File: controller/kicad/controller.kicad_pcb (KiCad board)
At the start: 2 copper layers, 90 x 88.4 mm, 33 parts, among them J1 pcie_98, J2 USB_C_Receptacle_USB2.0, U1 WeAct_STM32H750_Module, U10 ESD5344D, U11 ESD5344D, U12 ESD5344D, U13 ESD5344D, U14 ESD5344D, U15 ESD5344D, U16 CP2102N-A01-GQFN28-Interface_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, U2 ESD5344D, U3 ESD5344D, U4 ESD5344D, U5 ESD5344D, U6 ESD5344D, U7 ESD5344D, U8 ESD5344D, U9 ESD5344D

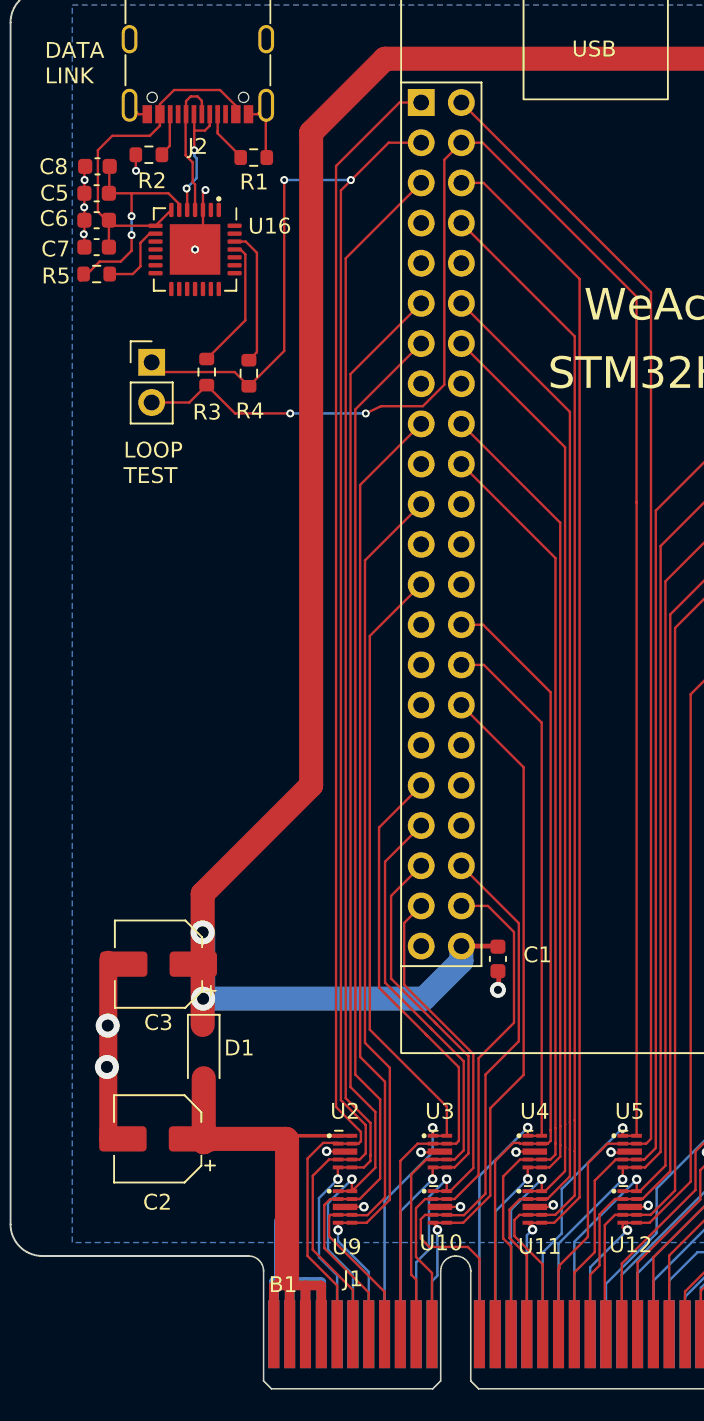
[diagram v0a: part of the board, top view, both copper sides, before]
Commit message: Cleaned up a few traces, move the power supply caps.
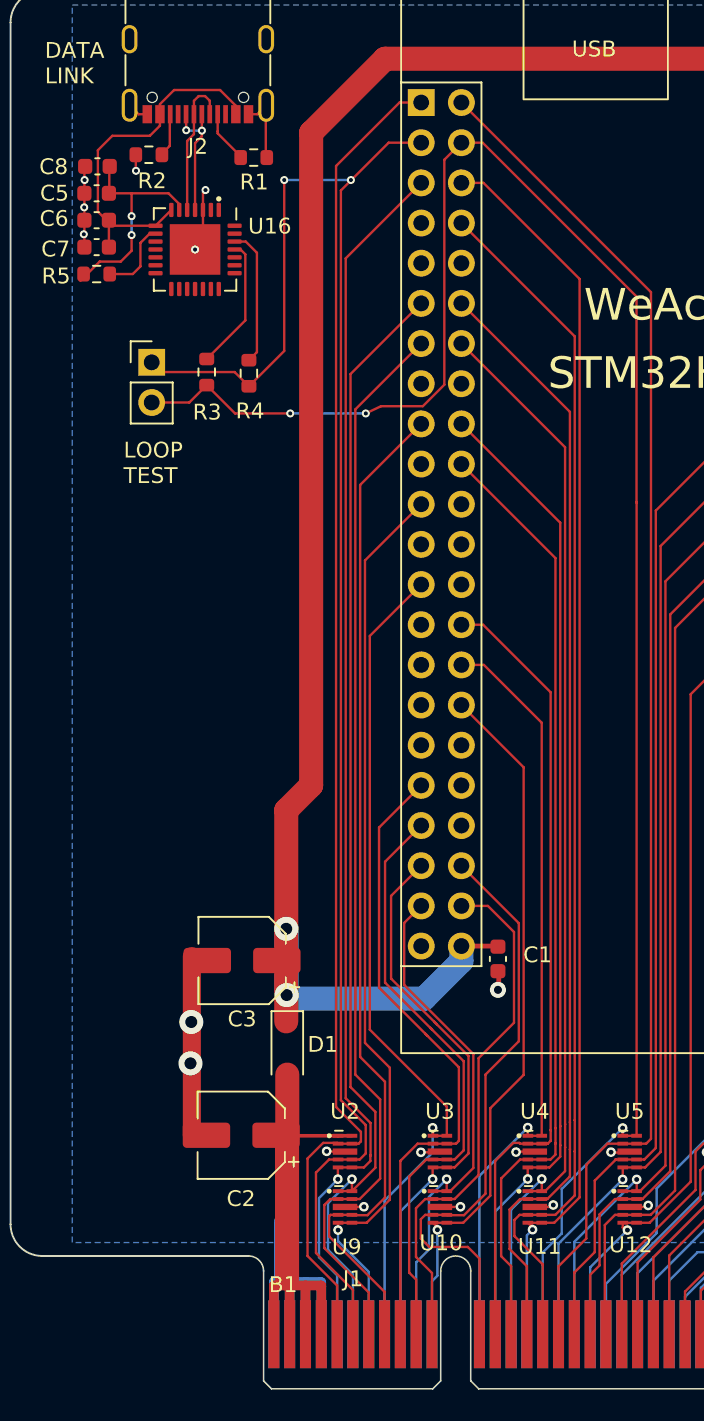
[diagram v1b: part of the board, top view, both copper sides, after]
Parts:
- moved C2 5.29 mm to (56.4, 44.0)
- moved C3 5.29 mm to (56.5, 32.9)
- moved D1 5.29 mm to (59.4, 38.5)
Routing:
- net /+5V: track 140.0 -> 132.4 mm
- net /+5VBUS: track 37.8 -> 32.5 mm
- net Net-(U16-D-): track 8.29 -> 9.17 mm, vias 2 -> 0
- net Net-(U16-D+): track 9.11 -> 8.25 mm, vias 0 -> 2

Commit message: Updated part number of a 1uf cap.
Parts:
- C1, C4: value 1uf -> 1u
- C2, C3: value 100uf -> 100u
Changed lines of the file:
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@@
     (descr "Capacitor SMD 0603 (1608 Metric), square (rectangular) end terminal, IPC_7351 nominal, (Body size source: IPC-SM-782 page 76, https://www.pcb-3d.com/wordpress/wp-content/uploads/ipc-sm-782a_amendment_1_and_2.pdf), generated with kicad-footprint-generator")
     (tags "capacitor")
-    (property "LCSC" "C106219")
+    (property "LCSC" "C15849")
     (property "Sheetfile" "controller.kicad_sch")
     (property "Sheetname" "")
@@
         (effects (font (size 1 1) (thickness 0.15)))
     )
-    (fp_text value "1uf" (at 0 1.43) (layer "F.Fab")
+    (fp_text value "1u" (at 0 1.43) (layer "F.Fab")
         (effects (font (size 1 1) (thickness 0.15)))
     )
@@
     (descr "Capacitor SMD 0603 (1608 Metric), square (rectangular) end terminal, IPC_7351 nominal, (Body size source: IPC-SM-782 page 76, https://www.pcb-3d.com/wordpress/wp-content/uploads/ipc-sm-782a_amendment_1_and_2.pdf), generated with kicad-footprint-generator")
     (tags "capacitor")
-    (property "LCSC" "C106219")
+    (property "LCSC" "C15849")
     (property "Sheetfile" "controller.kicad_sch")
     (property "Sheetname" "")
@@
         (effects (font (size 1 1) (thickness 0.15)))
     )
-    (fp_text value "1uf" (at 0 1.43 -90) (layer "F.Fab")
+    (fp_text value "1u" (at 0 1.43 -90) (layer "F.Fab")
         (effects (font (size 1 1) (thickness 0.15)))
     )
@@
         (effects (font (size 1 1) (thickness 0.15)))
     )
-    (fp_text value "100uf" (at 0 -3.7) (layer "F.Fab")
+    (fp_text value "100u" (at 0 -3.7) (layer "F.Fab")
         (effects (font (size 1 1) (thickness 0.15)))
     )
@@
         (effects (font (size 1 1) (thickness 0.15)))
     )
-    (fp_text value "100uf" (at 0 -3.7) (layer "F.Fab")
-        (effects (font (size 1 1) (thickness 0.15)))
-    )
+    (fp_text value "100u" (at 0 -3.7) (layer "F.Fab")
+        (effects (font (size 1 1) (thickness 0.15)))
+    )

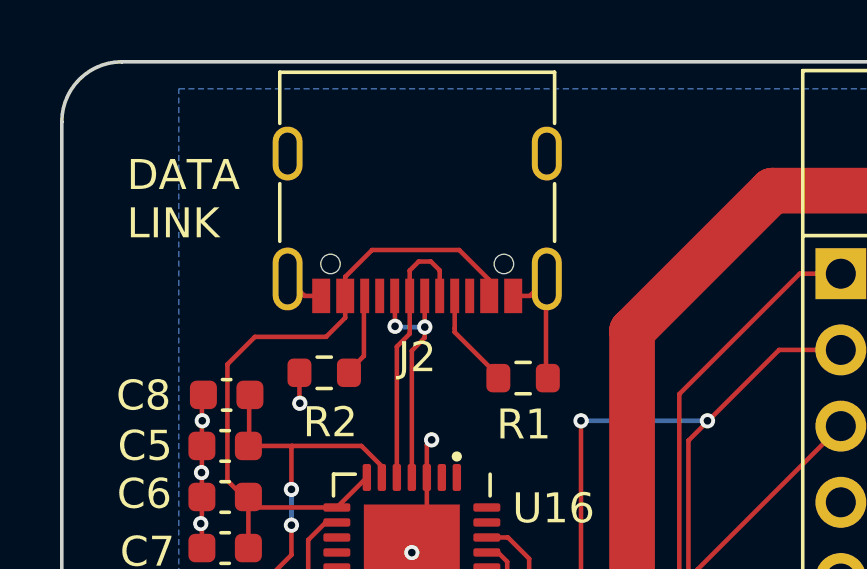
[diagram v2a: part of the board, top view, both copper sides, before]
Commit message: Moved the USB connector closer to the board edge.
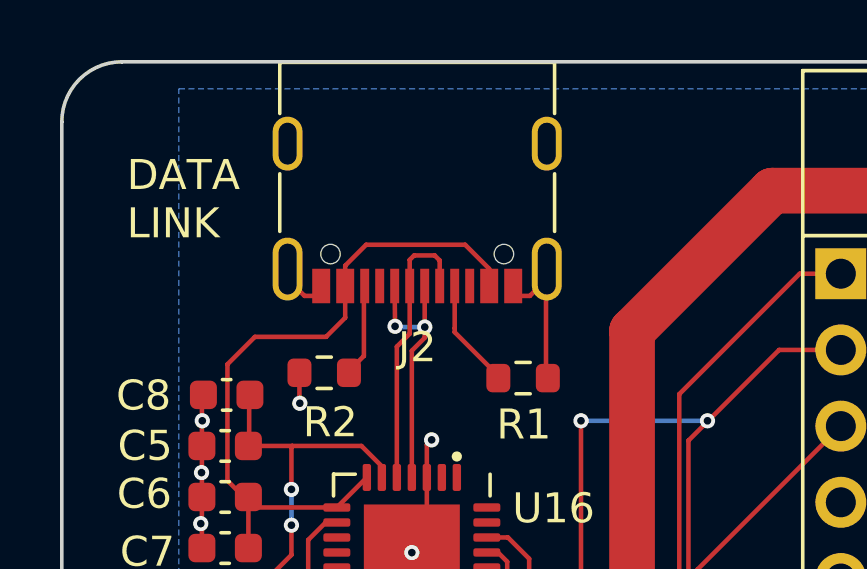
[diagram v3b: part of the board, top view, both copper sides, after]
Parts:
- moved J2 0.33 mm to (53.7, -23.1)
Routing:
- net Net-(J2-VBUS): track 23.1 -> 23.6 mm
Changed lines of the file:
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@@
   )
   (footprint "controller:USB_C_Receptacle_XKB_U262-16XN-4BVC11" (layer "F.Cu")
-    (at 53.6967 -22.7663 180)
+    (at 53.6967 -23.0965 180)
     (descr "USB Type C, right-angle, SMT, https://datasheet.lcsc.com/szlcsc/1811141824_XKB-Enterprise-U262-161N-4BVC11_C319148.pdf")
     (tags "USB C Type-C Receptacle SMD")
@@
   (via (at 49.5046 -14.1478) (size 0.508) (drill 0.254) (layers "F.Cu" "B.Cu") (net 120))
   (segment (start 49.5046 -12.954) (end 49.5046 -14.1478) (width 0.1524) (layer "B.Cu") (net 120))
+  (segment (start 48.2865 -19.2315) (end 47.371 -18.316) (width 0.1524) (layer "F.Cu") (net 121))
   (segment (start 47.371 -18.316) (end 47.371 -14.4402) (width 0.1524) (layer "F.Cu") (net 121))
-  (segment (start 56.0967 -21.1285) (end 55.0981 -22.1271) (width 0.1524) (layer "F.Cu") (net 121))
-  (segment (start 51.2967 -20.5963) (end 51.2967 -19.8689) (width 0.1524) (layer "F.Cu") (net 121))
-  (segment (start 56.0967 -20.5963) (end 56.0967 -21.1285) (width 0.1524) (layer "F.Cu") (net 121))
-  (segment (start 51.2967 -21.230364) (end 51.2967 -20.5963) (width 0.1524) (layer "F.Cu") (net 121))
-  (segment (start 55.0981 -22.1271) (end 52.193436 -22.1271) (width 0.1524) (layer "F.Cu") (net 121))
+  (segment (start 55.2958 -22.3012) (end 51.9938 -22.3012) (width 0.1524) (layer "F.Cu") (net 121))
+  (segment (start 47.371 -14.4402) (end 48.2671 -13.5441) (width 0.1524) (layer "F.Cu") (net 121))
   (segment (start 48.2671 -13.5441) (end 51.0178 -13.5441) (width 0.1524) (layer "F.Cu") (net 121))
+  (segment (start 51.2967 -21.6041) (end 51.2967 -20.9265) (width 0.1524) (layer "F.Cu") (net 121))
+  (segment (start 51.2967 -21.230364) (end 51.2967 -19.8689) (width 0.1524) (layer "F.Cu") (net 121))
+  (segment (start 56.0967 -21.5003) (end 55.2958 -22.3012) (width 0.1524) (layer "F.Cu") (net 121))
+  (segment (start 52.0178 -14.5441) (end 51.0178 -13.5441) (width 0.1524) (layer "F.Cu") (net 121))
+  (segment (start 56.0967 -20.9265) (end 56.0967 -21.5003) (width 0.1524) (layer "F.Cu") (net 121))
+  (segment (start 48.0698 -13.8938) (end 48.0698 -12.192) (width 0.1524) (layer "F.Cu") (net 121))
   (segment (start 50.6593 -19.2315) (end 48.2865 -19.2315) (width 0.1524) (layer "F.Cu") (net 121))
   (segment (start 51.2967 -19.8689) (end 50.6593 -19.2315) (width 0.1524) (layer "F.Cu") (net 121))
-  (segment (start 47.371 -14.4402) (end 48.2671 -13.5441) (width 0.1524) (layer "F.Cu") (net 121))
-  (segment (start 52.193436 -22.1271) (end 51.2967 -21.230364) (width 0.1524) (layer "F.Cu") (net 121))
-  (segment (start 48.2865 -19.2315) (end 47.371 -18.316) (width 0.1524) (layer "F.Cu") (net 121))
-  (segment (start 52.0178 -14.5441) (end 51.0178 -13.5441) (width 0.1524) (layer "F.Cu") (net 121))
-  (segment (start 48.0698 -13.8938) (end 48.0698 -12.192) (width 0.1524) (layer "F.Cu") (net 121))
+  (segment (start 51.9938 -22.3012) (end 51.2967 -21.6041) (width 0.1524) (layer "F.Cu") (net 121))
   (segment (start 54.9467 -19.5187) (end 54.9467 -19.3869) (width 0.1524) (layer "F.Cu") (net 122))
   (segment (start 54.9467 -20.5963) (end 54.9467 -19.5187) (width 0.1524) (layer "F.Cu") (net 122))
@@
   (segment (start 53.9496 -19.558) (end 52.9844 -19.558) (width 0.1524) (layer "B.Cu") (net 124))
   (segment (start 52.9844 -19.558) (end 52.959 -19.5834) (width 0.1524) (layer "B.Cu") (net 124))
-  (segment (start 53.7464 -21.7424) (end 53.4467 -21.4427) (width 0.1524) (layer "F.Cu") (net 125))
-  (segment (start 54.4467 -21.4485) (end 54.1528 -21.7424) (width 0.1524) (layer "F.Cu") (net 125))
+  (segment (start 54.4467 -21.7787) (end 54.2798 -21.9456) (width 0.1524) (layer "F.Cu") (net 125))
   (segment (start 53.0178 -18.9056) (end 53.4467 -19.3345) (width 0.1524) (layer "F.Cu") (net 125))
-  (segment (start 54.4467 -20.5963) (end 54.4467 -21.4485) (width 0.1524) (layer "F.Cu") (net 125))
-  (segment (start 54.1528 -21.7424) (end 53.7464 -21.7424) (width 0.1524) (layer "F.Cu") (net 125))
-  (segment (start 53.4467 -21.4427) (end 53.4467 -20.5963) (width 0.1524) (layer "F.Cu") (net 125))
+  (segment (start 53.4467 -21.7983) (end 53.4467 -20.9265) (width 0.1524) (layer "F.Cu") (net 125))
+  (segment (start 54.4467 -20.9265) (end 54.4467 -21.7787) (width 0.1524) (layer "F.Cu") (net 125))
+  (segment (start 54.2798 -21.9456) (end 53.594 -21.9456) (width 0.1524) (layer "F.Cu") (net 125))
+  (segment (start 53.594 -21.9456) (end 53.4467 -21.7983) (width 0.1524) (layer "F.Cu") (net 125))
   (segment (start 53.4467 -19.3345) (end 53.4467 -20.5963) (width 0.1524) (layer "F.Cu") (net 125))
   (segment (start 53.0178 -14.5441) (end 53.0178 -18.9056) (width 0.1524) (layer "F.Cu") (net 125))

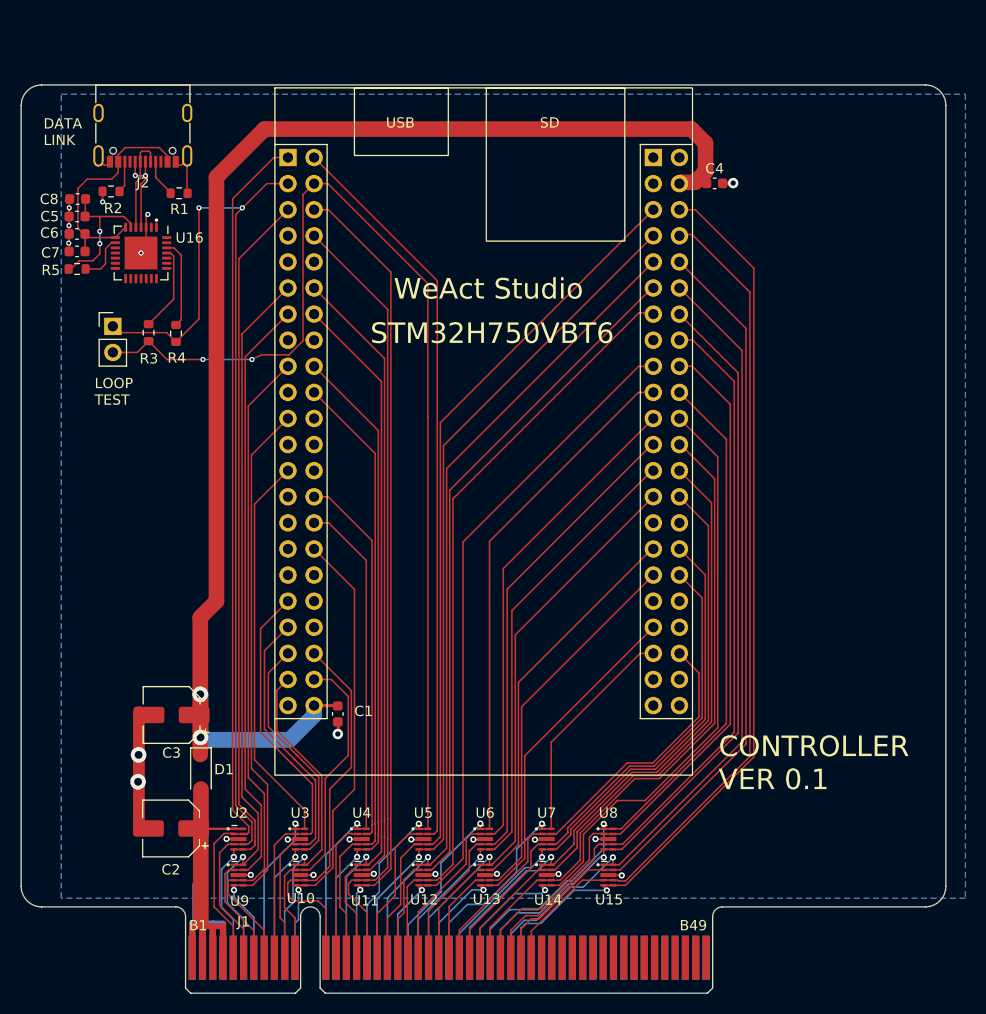
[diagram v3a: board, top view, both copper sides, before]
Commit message: Cleaning up of the controller's PCB, in progress.
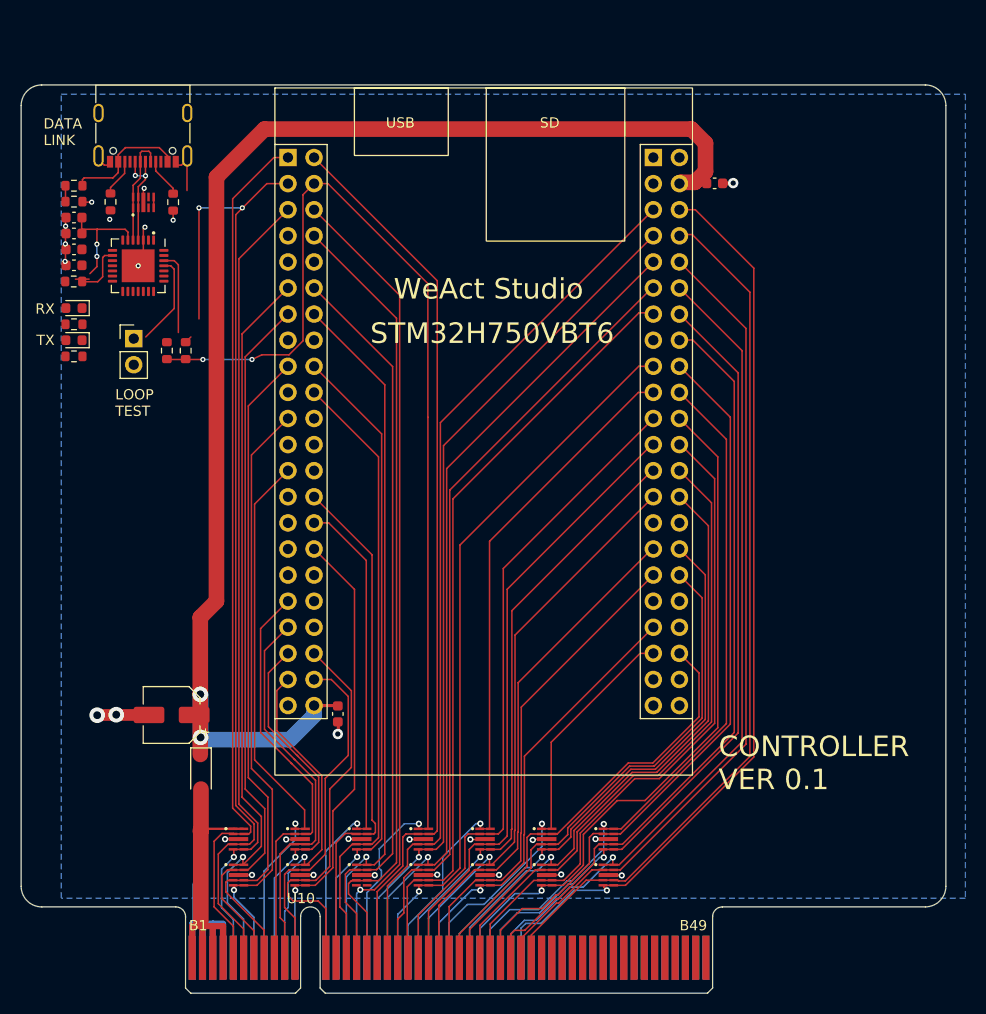
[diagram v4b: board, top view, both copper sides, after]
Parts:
- removed C2: 100u, controller:CP_Elec_5x5.4_JLCPCB
- added D2: LED YELLOW, LED_SMD:LED_0603_1608Metric, F.Cu at (47.0, -3.56)
- added D3: LED_GREEN, LED_SMD:LED_0603_1608Metric, F.Cu at (47.0, -6.68)
- added R6: 47K, Resistor_SMD:R_0603_1608Metric, F.Cu at (47.0, -17.0)
- added R7: 22K, Resistor_SMD:R_0603_1608Metric, F.Cu at (47.0, -18.6)
- added R8: 5K1, Resistor_SMD:R_0603_1608Metric, F.Cu at (47.0, -1.98)
- added R9: 5K1, Resistor_SMD:R_0603_1608Metric, F.Cu at (47.0, -5.11)
- added U17: ESD5344D, common:Diodes_UDFN-10_1.0x2.5mm_P0.5mm, F.Cu at (53.7, -17.0)
- U16: value CP2102N-A01-GQFN28-Interface_USB -> CP2102N-A02-GQFN28R
- moved R3 2.50 mm to (56.0, -2.54)
- moved JP1 2.36 mm to (52.8, -3.71)
- moved R4 1.92 mm to (57.9, -2.54)
- moved C8 1.84 mm to (47.0, -15.5)
- moved C5 1.68 mm to (47.0, -13.9)
- moved C6 1.53 mm to (47.0, -12.4)
- moved C7 1.38 mm to (47.0, -10.8)
- moved U16 1.28 mm to (53.2, -10.8)
- moved R5 1.26 mm to (47.0, -9.27)
- moved R1 1.04 mm to (56.6, -17.0), turned to -90 degrees
- moved R2 1.02 mm to (50.5, -17.0), turned to -90 degrees
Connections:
- C6 pad 2: Net-(J2-VBUS) -> /+5V
- C7 pad 2: Net-(J2-VBUS) -> /+5V
- JP1 pad 1: /PB15 -> /PA10
- JP1 pad 2: /PB14 -> /PA9
- R3 pad 2: /PB14 -> /PA9
- R4 pad 2: /PB15 -> /PA10
- U1 pad 80: unconnected-(U1B-NRST-Pad80) -> /NRST
- U16 pad 18: unconnected-(U16-~{RXT}/GPIO.1-Pad18) -> Net-(D3-K)
- U16 pad 19: unconnected-(U16-~{TXT}/GPIO.0-Pad19) -> Net-(D2-K)
- U16 pad 7: Net-(J2-VBUS) -> /+5V
- U16 pad 8: Net-(J2-VBUS) -> Net-(U16-VBUS)
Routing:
- net Net-(J2-VBUS): track 23.6 -> 12.4 mm
- net /PB15: track 107.7 -> 98.1 mm
- net /PB14: track 120.8 -> 115.3 mm
- net GND: track 65.7 -> 61.7 mm, vias 24 -> 27
- net Net-(U16-VDD): track 14.8 -> 12.0 mm
- net Net-(U16-~{RSTb}): track 4.83 -> 6.39 mm
- net Net-(U16-VBUS): track 0.00 -> 1.55 mm
- net Net-(U16-D+): track 8.25 -> 9.61 mm
- net Net-(U16-D-): track 9.08 -> 10.4 mm
- net /PD14: track 71.1 -> 72.4 mm
- net unconnected-(U17-D4-Pad5): track 0.00 -> 1.05 mm
- net /PD10: track 76.9 -> 77.8 mm
- net /PA4: track 60.2 -> 60.9 mm
- net /PA9: track 64.1 -> 64.9 mm
- net /PA15: track 57.5 -> 58.2 mm
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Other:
- board text added: "RX"
- board text added: "TX"
